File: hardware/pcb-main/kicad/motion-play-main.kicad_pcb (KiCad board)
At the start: 4 copper layers, 83.9 x 39.1 mm, 92 parts, among them IC1 SN74AHCT125PWR, J3 LED_Strip, J4 Conn_01x04, J5 Conn_01x04, J6 Conn_01x04, J7 TYPE-C-31-M-12, J8 JST_PH_2pin, Q2 PMOS, SW1 SS-12D10L5, SW2 RESET, SW3 BOOT, U3 ESP32-S3-WROOM-1-N16R8, U4 TCA9548APWR, U5 BQ24195RGER, U6 TPS61088RHLR, U7 INA219AIDCNR, U8 AMS1117-3.3, U9 USBLC6-2SC6

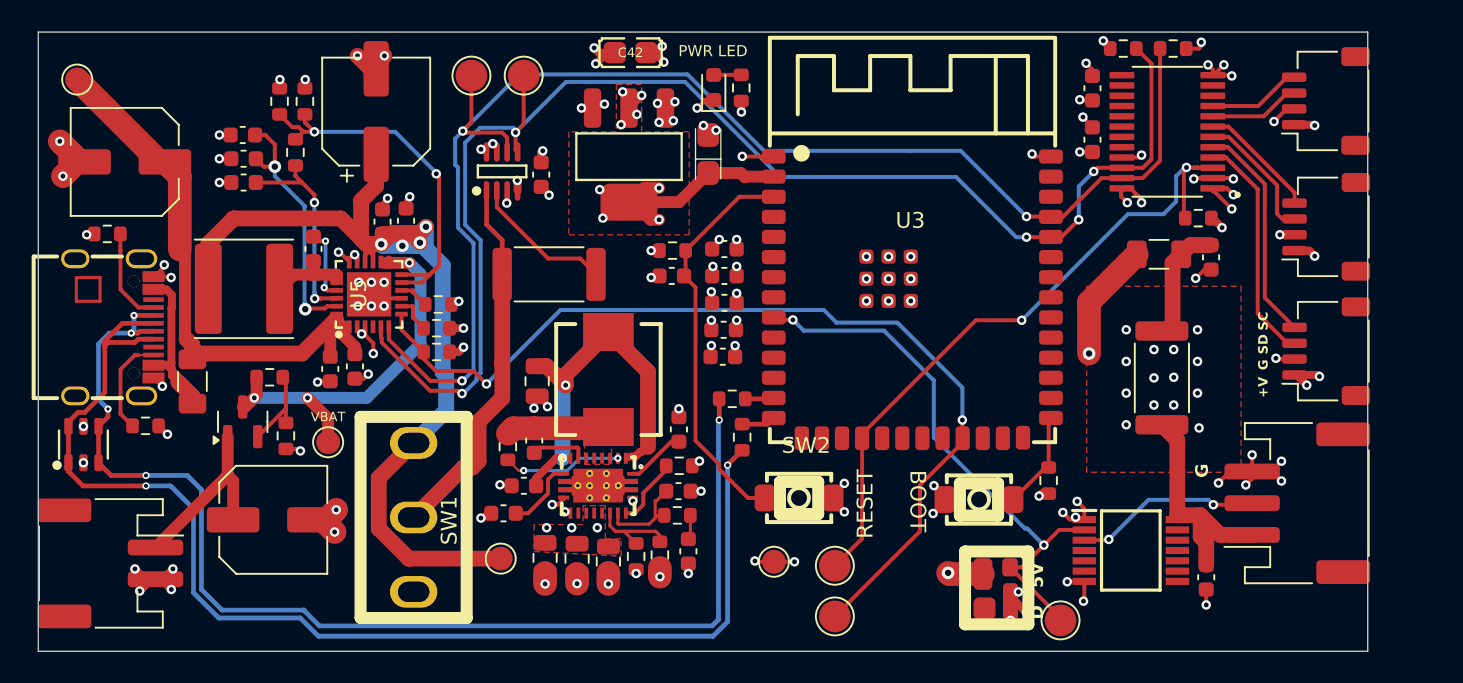
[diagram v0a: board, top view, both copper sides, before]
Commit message: Main PCB v7 finalization: schematic, layout, production files, and reports
Includes power management schematic updates, PCB layout changes,
updated BOM/positions/netlist for JLCPCB fabrication, DRC/ERC reports,
slide switch footprint library addition, and review handoff docs.

Co-Authored-By: Claude Opus 4.6 (1M context) <noreply@anthropic.com>
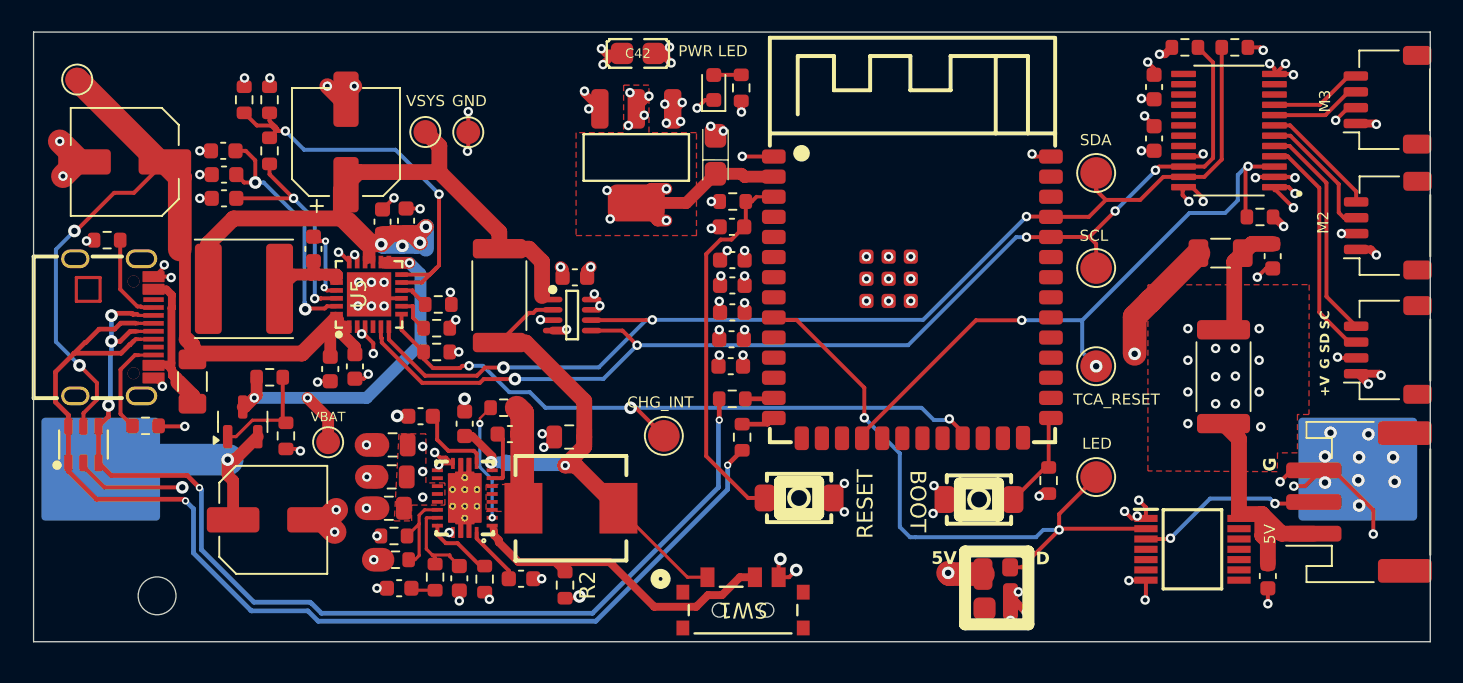
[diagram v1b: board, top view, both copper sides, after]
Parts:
- removed J8: JST_PH_2pin, Connector_JST:JST_PH_S2B-PH-SM4-TB_1x02-1MP_P2.00mm_Horizontal
- added BT1: Battery_Cell, Battery:BatteryHolder_Keystone_1042_1x18650, B.Cu at (119.6, 128.6)
- added R2: 100kΩ, Resistor_SMD:R_0603_1608Metric, F.Cu at (109.3, 135.9)
- SW1: value SS-12D10L5 -> SW_SPDT; footprint JLC-MCP:SW-TH_SS-12D10L5 -> JLC-MCP:MK-12C02-G020_GSW
- moved TPIO43 39.9 mm to (142.8, 109.9)
- moved TPIO44 38.1 mm to (142.8, 115.9)
- moved TP4 33.3 mm to (103.2, 107.3), turned to 180 degrees
- moved TP1 27.4 mm to (100.4, 107.3)
- moved SW1 21.6 mm to (120.5, 137.5), turned to 0 degrees
- moved TPIO10 20.8 mm to (142.8, 122.1)
- moved C38 18.4 mm to (98.8, 136.1), turned to 180 degrees
- moved R39 16.7 mm to (98.6, 134.3), turned to 0 degrees
- moved R43 15.8 mm to (101.1, 135.4), turned to -90 degrees
- moved TPIO21 15.7 mm to (115.5, 126.5)
- moved R40 15.3 mm to (98.5, 132.8), turned to 180 degrees
- moved C39 14.9 mm to (102.6, 135.5), turned to -90 degrees
- moved C36 14.3 mm to (98.1, 131.1), turned to 180 degrees
- moved R42 14.2 mm to (104.2, 135.5), turned to -90 degrees
- moved C33 13.7 mm to (106.5, 135.5), turned to 0 degrees
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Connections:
- Q2 pad 1: /Power Management/BAT_RAW -> /Power Management/PMOS_GATE
- Q2 pad 2: /Power Management/PMOS_GATE -> /Power Management/BAT_RAW
- R44 pad 1: /Power Management/VSYS_SW -> /Power Management/VSYS
- SW1 pad 1: /Power Management/VSYS -> /Power Management/VSYS_SENSE
- SW1 pad 2: /Power Management/VSYS_SW -> /Power Management/BOOST_EN
- SW1 pad 3: unconnected-(SW1-Pad3) -> GND
- U6 pad 2: /Power Management/VSYS_SENSE -> /Power Management/BOOST_EN
- U7 pad 1: /Power Management/VSYS_SW -> /Power Management/VSYS
- U9 pad 5: GND -> /Power Management/Protected_VBUS
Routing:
- net GND: track 104.9 -> 134.0 mm, vias 131 -> 136
- net /Power Management/VSYS_SW: track 23.8 -> 0.00 mm
- net /Power Management/Protected_VBUS: track 35.9 -> 57.7 mm, vias 0 -> 2
- net /Power Management/BOOST_EN: track 0.00 -> 20.9 mm
- net /CHRG_INT: track 59.8 -> 42.8 mm, vias 2 -> 3
- net /I2C_SDA: track 89.2 -> 72.9 mm
- net /I2C_SCL: track 89.3 -> 73.3 mm
- net /Power Management/VSYS: track 67.0 -> 52.9 mm
- net /LED_DATA: track 35.8 -> 42.1 mm
- net /USB_DN: track 75.7 -> 69.6 mm
- net /USB_DP: track 77.1 -> 73.0 mm
- net /Power Management/BAT_RAW: track 11.8 -> 14.7 mm, vias 0 -> 1
- net /Power Management/BQ_TS: track 24.6 -> 26.8 mm
- net /TCA_RESET: track 42.7 -> 40.8 mm, vias 2 -> 3
- net /Power Management/BQ_REGN: track 13.2 -> 14.7 mm
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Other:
- board size 83.9 x 39.1 mm -> 88.2 x 38.5 mm
- board text added: "CHG_INT"
- board text added: "GND"
- board text added: "LED"
- board text added: "M2"
- board text added: "M3"
- board text added: "SCL"
- board text added: "SDA"
- board text added: "TCA_RESET"
- board text added: "VSYS"
